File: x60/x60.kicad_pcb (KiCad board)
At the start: 2 copper layers, 285.7 x 95.2 mm, 150 parts, among them SW1 SW_Push, U1 ATmega32U4-AU, Y1 16mhz

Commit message: decoration
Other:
- board text added: "x60 PCB Rev. 0 by x45#0283"
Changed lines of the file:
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@@
   (general
     (thickness 1.6)
-    (drawings 5)
+    (drawings 6)
     (tracks 1058)
     (zones 0)
@@
     )
   )
+  (gr_text "x60 PCB Rev. 0 by x45#0283" (at 331.945 202.715) (layer F.SilkS)
+    (effects (font (size 2 2) (thickness 0.15)))
+  )
   (gr_line (start 69.325 204.405) (end 355.025 204.425) (layer Edge.Cuts) (width 0.05))

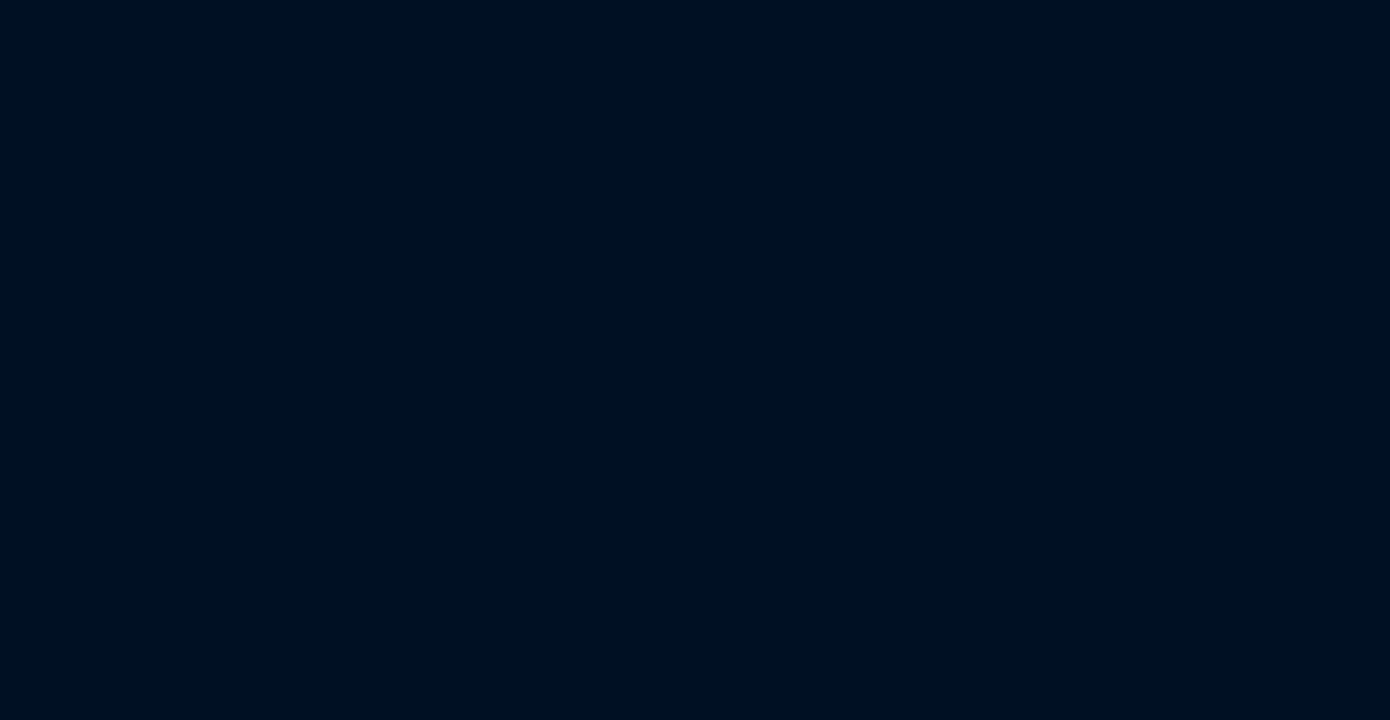
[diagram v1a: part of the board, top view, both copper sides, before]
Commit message: redid usbc integration
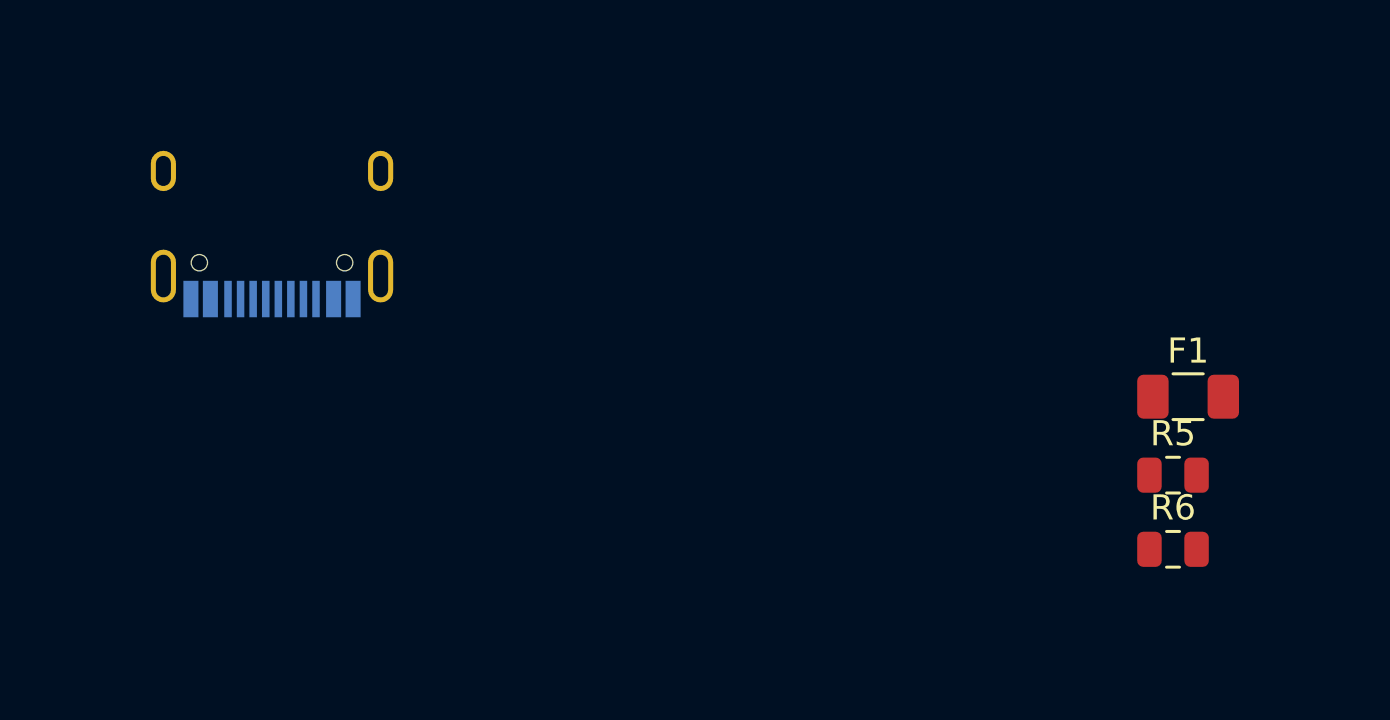
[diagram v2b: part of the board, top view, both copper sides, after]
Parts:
- added F1: 500mA, Fuse:Fuse_1206_3216Metric, F.Cu at (212.0, 243.1)
- added R5: 5k, Resistor_SMD:R_0805_2012Metric, F.Cu at (211.4, 246.2)
- added R6: 5k, Resistor_SMD:R_0805_2012Metric, F.Cu at (211.4, 249.2)
- added USB1: HRO-TYPE-C-31-M-12, Type-C:HRO-TYPE-C-31-M-12, B.Cu at (175.5, 231.5)
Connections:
- C1 pad 2: GND -> D+
- C2 pad 2: GND -> D+
- C3 pad 2: GND -> D+
- C4 pad 2: GND -> D+
- C5 pad 2: GND -> D+
- C6 pad 2: GND -> D+
- C7 pad 2: GND -> D+
- R4 pad 1: GND -> D+
- SW1 pad 1: GND -> D+
- U1 pad 15: GND -> D+
- U1 pad 23: GND -> D+
- U1 pad 35: GND -> D+
- U1 pad 43: GND -> D+
- U1 pad 5: GND -> D+
- Y1 pad 2: GND -> D+
- Y1 pad 4: GND -> D+
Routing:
- net GND: track 106.9 -> 0.00 mm
- net D+: track 0.00 -> 106.9 mm

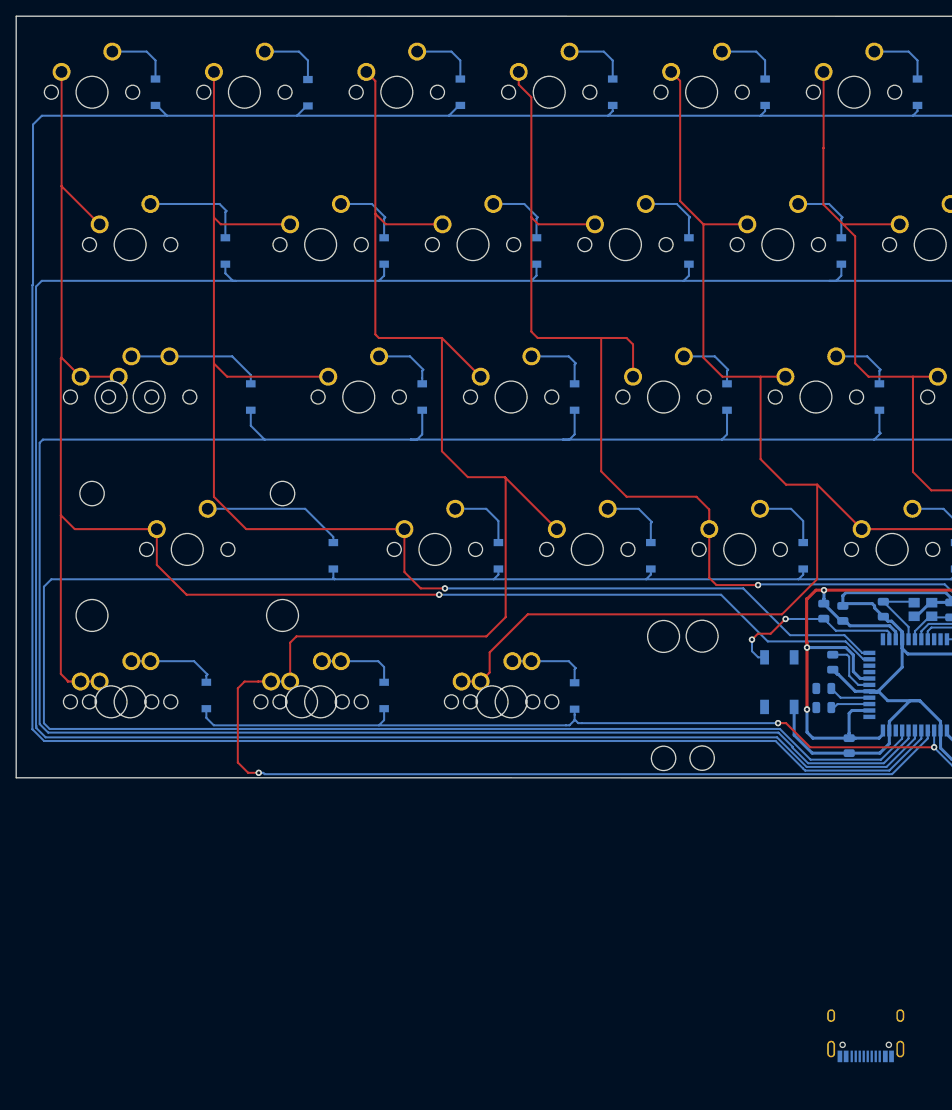
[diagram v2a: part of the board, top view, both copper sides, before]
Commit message: usb c port placement
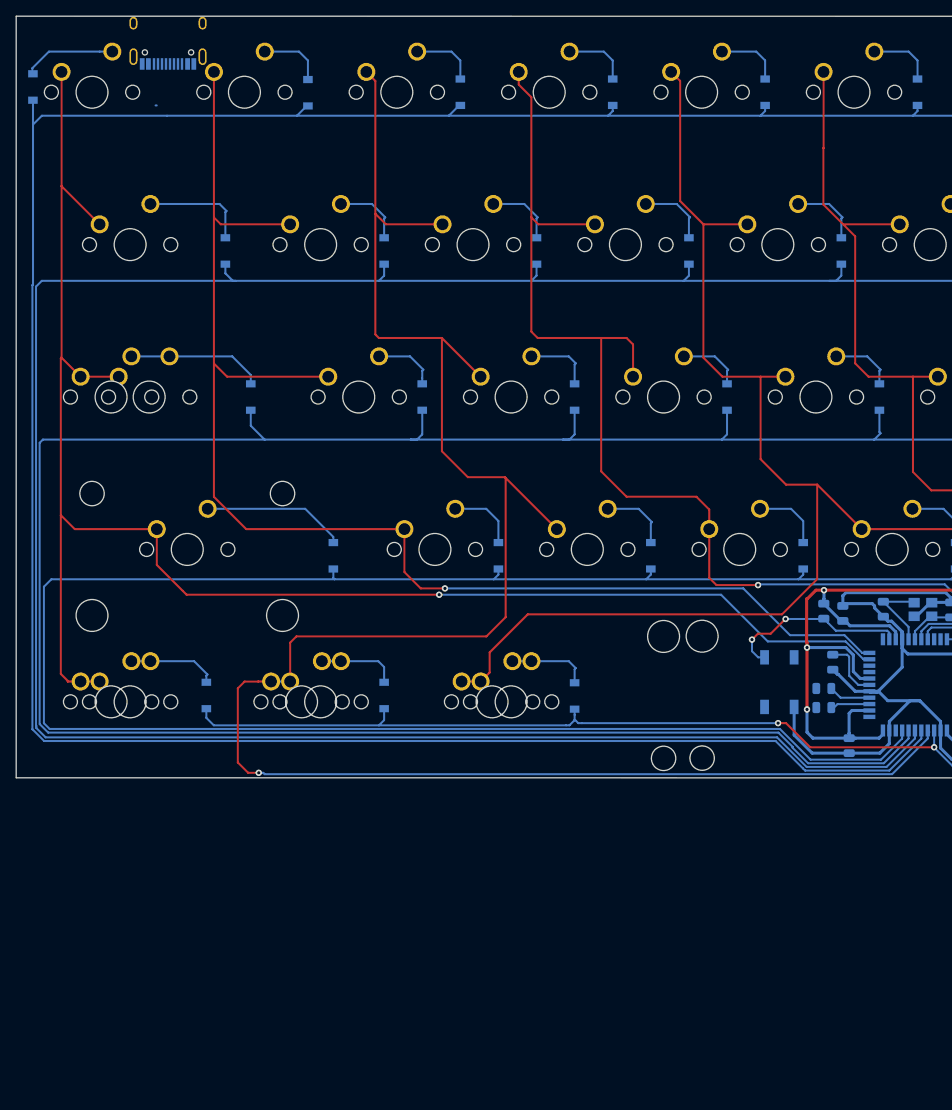
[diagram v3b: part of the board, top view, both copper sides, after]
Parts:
- moved USB1 151.6 mm to (88.3, 107.5)
- moved D1 15.3 mm to (71.4, 118.1)
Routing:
- net Net-(D1-Pad2): track 8.18 -> 11.6 mm
- net ROW1: track 462.7 -> 464.0 mm
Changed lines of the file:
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@@
     (thickness 1.6)
     (drawings 6)
-    (tracks 1058)
+    (tracks 1061)
     (zones 0)
     (modules 154)
@@
   )
   (module Type-C:HRO-TYPE-C-31-M-12 (layer B.Cu)
-    (at 175.515 231.535)
+    (at 88.3 107.48)
     (attr smd)
     (fp_text reference USB1 (at 0 9.25) (layer B.SilkS)
@@
   )
   (module Diode_SMD:D_SOD-123 (layer B.Cu)
-    (at 86.74125 118.70875 90)
+    (at 71.415 118.055 90)
     (descr SOD-123)
     (tags SOD-123)
@@
   (segment (start 173.45 191.65375) (end 174.5875 192.79125) (width 0.254) (layer B.Cu) (net 4))
   (segment (start 173.45 189.2725) (end 173.45 191.65375) (width 0.254) (layer B.Cu) (net 4))
-  (segment (start 81.34375 113.62875) (end 85.63 113.62875) (width 0.254) (layer B.Cu) (net 5))
-  (segment (start 85.63 113.62875) (end 86.74125 114.74) (width 0.254) (layer B.Cu) (net 5))
-  (segment (start 86.74125 114.74) (end 86.74125 117.05875) (width 0.254) (layer B.Cu) (net 5))
+  (segment (start 79.75276 113.62875) (end 81.34375 113.62875) (width 0.254) (layer B.Cu) (net 5))
+  (segment (start 73.41725 113.62875) (end 79.75276 113.62875) (width 0.254) (layer B.Cu) (net 5))
+  (segment (start 71.345 115.701) (end 73.41725 113.62875) (width 0.254) (layer B.Cu) (net 5))
+  (segment (start 71.345 116.405) (end 71.345 115.701) (width 0.254) (layer B.Cu) (net 5))
   (segment (start 105.64125 120.42125) (end 105.79125 120.42125) (width 0.254) (layer B.Cu) (net 6))
   (segment (start 104.41625 121.64625) (end 105.64125 120.42125) (width 0.254) (layer B.Cu) (net 6))
   (segment (start 88.17875 121.64625) (end 104.41625 121.64625) (width 0.254) (layer B.Cu) (net 6))
-  (segment (start 86.89125 120.35875) (end 88.17875 121.64625) (width 0.254) (layer B.Cu) (net 6))
   (segment (start 86.74125 120.35875) (end 86.89125 120.35875) (width 0.254) (layer B.Cu) (net 6))
   (segment (start 124.69125 120.35875) (end 124.84125 120.35875) (width 0.254) (layer B.Cu) (net 6))
@@
   (segment (start 167.941156 203.49904) (end 167.675203 203.233086) (width 0.254) (layer B.Cu) (net 6))
   (segment (start 167.675203 203.233086) (end 164.249444 199.807327) (width 0.254) (layer B.Cu) (net 6))
-  (segment (start 71.4275 142.739183) (end 71.4275 122.75125) (width 0.254) (layer B.Cu) (net 6))
   (segment (start 72.82151 199.807327) (end 71.34948 198.335297) (width 0.254) (layer B.Cu) (net 6))
   (segment (start 164.249444 199.807327) (end 72.82151 199.807327) (width 0.254) (layer B.Cu) (net 6))
+  (segment (start 71.425 120.395) (end 71.425 119.691) (width 0.254) (layer B.Cu) (net 6))
+  (segment (start 71.425 122.821) (end 71.425 120.395) (width 0.254) (layer B.Cu) (net 6))
+  (segment (start 71.4275 122.9175) (end 71.4275 122.75125) (width 0.254) (layer B.Cu) (net 6))
+  (segment (start 71.4275 142.739183) (end 71.4275 122.9175) (width 0.254) (layer B.Cu) (net 6))
   (segment (start 86.10625 132.67875) (end 94.7425 132.67875) (width 0.254) (layer B.Cu) (net 7))
   (segment (start 94.7425 132.67875) (end 95.61625 133.5525) (width 0.254) (layer B.Cu) (net 7))

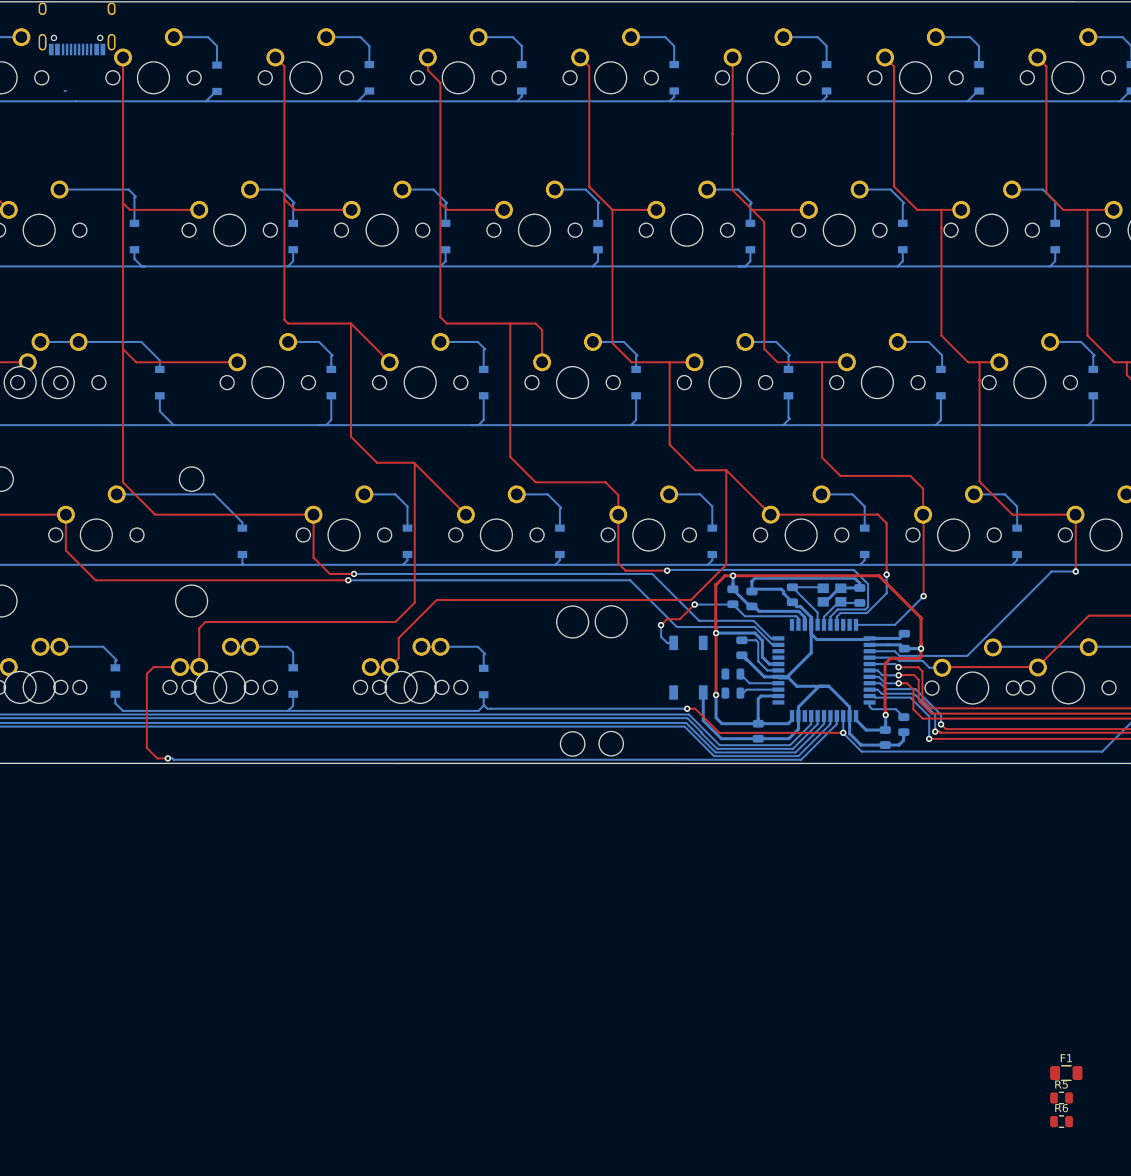
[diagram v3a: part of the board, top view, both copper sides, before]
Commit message: wired usb port
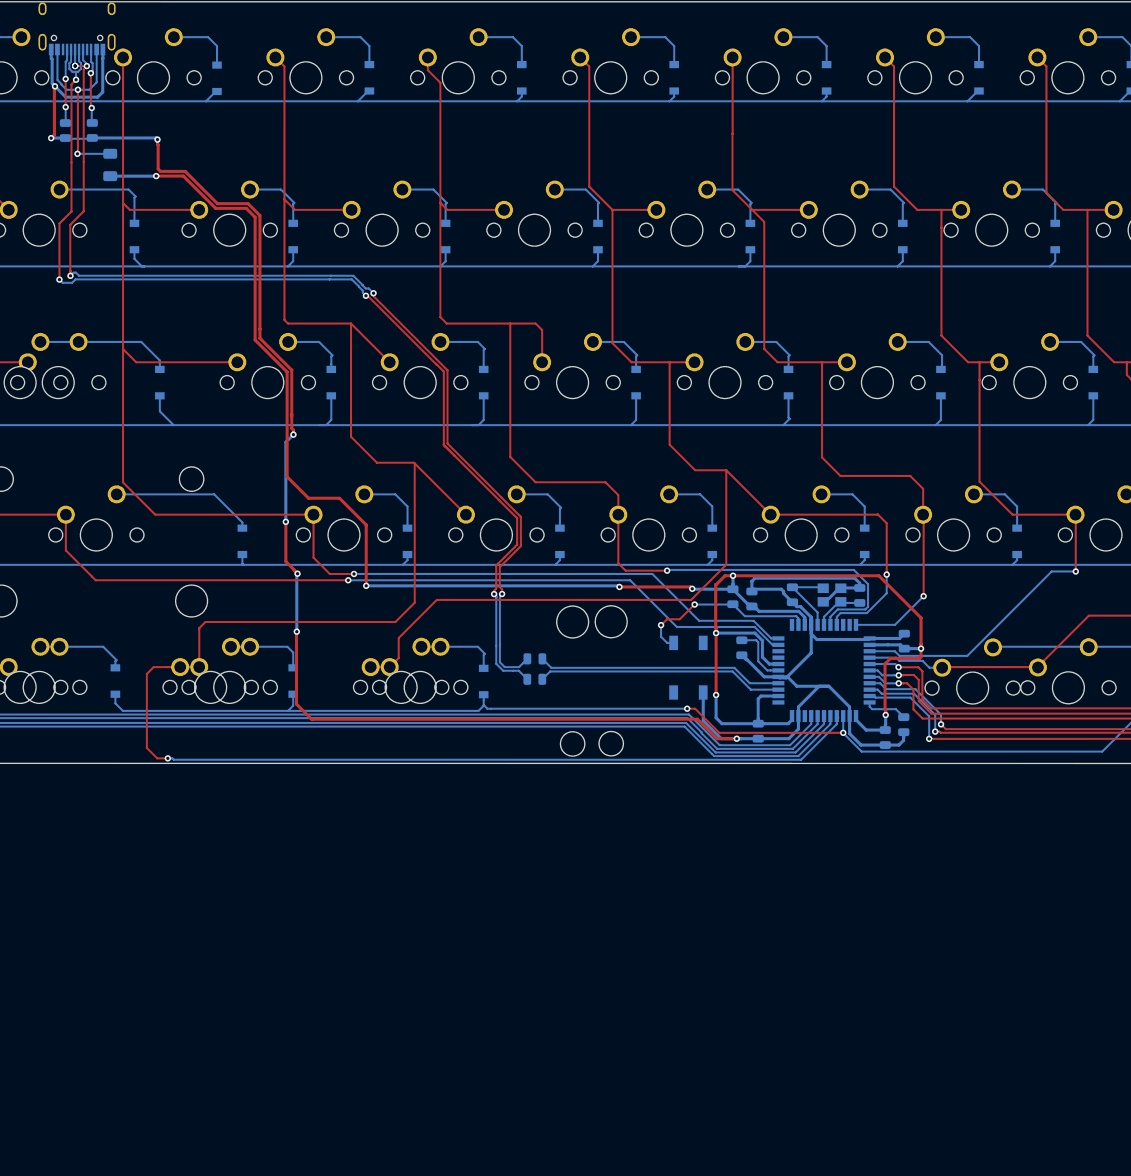
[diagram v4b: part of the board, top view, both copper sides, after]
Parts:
- F1, R5, R6: moved to B.Cu
- moved R5 173.6 mm to (86.8, 125.3), turned to 90 degrees
- moved R6 173.3 mm to (90.2, 125.3), turned to 90 degrees
- moved F1 164.8 mm to (92.4, 129.6), turned to 90 degrees
- moved R2 24.8 mm to (145.5, 191.3)
- moved R1 24.8 mm to (145.5, 193.9)
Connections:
- C1 pad 2: D+ -> GND
- C2 pad 2: D+ -> GND
- C3 pad 2: D+ -> GND
- C4 pad 2: D+ -> GND
- C5 pad 2: D+ -> GND
- C6 pad 2: D+ -> GND
- C7 pad 2: D+ -> GND
- R4 pad 1: D+ -> GND
- R5 pad 1: D+ -> GND
- R6 pad 1: D+ -> GND
- SW1 pad 1: D+ -> GND
- U1 pad 15: D+ -> GND
- U1 pad 23: D+ -> GND
- U1 pad 35: D+ -> GND
- U1 pad 43: D+ -> GND
- U1 pad 5: D+ -> GND
- USB1 pad 1: D+ -> GND
- USB1 pad 12: D+ -> GND
- Y1 pad 2: D+ -> GND
- Y1 pad 4: D+ -> GND
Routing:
- net GND: track 0.00 -> 284.1 mm, vias 0 -> 8
- net D-: track 0.00 -> 136.5 mm, vias 0 -> 4
- net +5V: track 114.9 -> 235.2 mm, vias 5 -> 9
- net Net-(R1-Pad1): track 4.86 -> 30.9 mm
- net VCC: track 0.00 -> 25.9 mm, vias 0 -> 2
- net Net-(R2-Pad1): track 5.23 -> 30.8 mm
- net D+: track 106.9 -> 132.3 mm, vias 0 -> 6
- net Net-(R6-Pad2): track 0.00 -> 9.43 mm, vias 0 -> 2
- net Net-(R5-Pad2): track 0.00 -> 9.31 mm, vias 0 -> 2

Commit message: generated gerbers
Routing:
- net +5V: track 235.2 -> 237.0 mm
